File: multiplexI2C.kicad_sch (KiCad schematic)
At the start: 27 parts, among them J17 Conn_01x04_Pin, J18 PinSocket_1x20_P2.54mm_Vertic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, J19 PinSocket_1x20_P2.54mm_Vertic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, J20 Screw_Terminal_01x02, J9 header_0.25sqmm_1x04_P4.2mm_D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, U1 TCA9548A

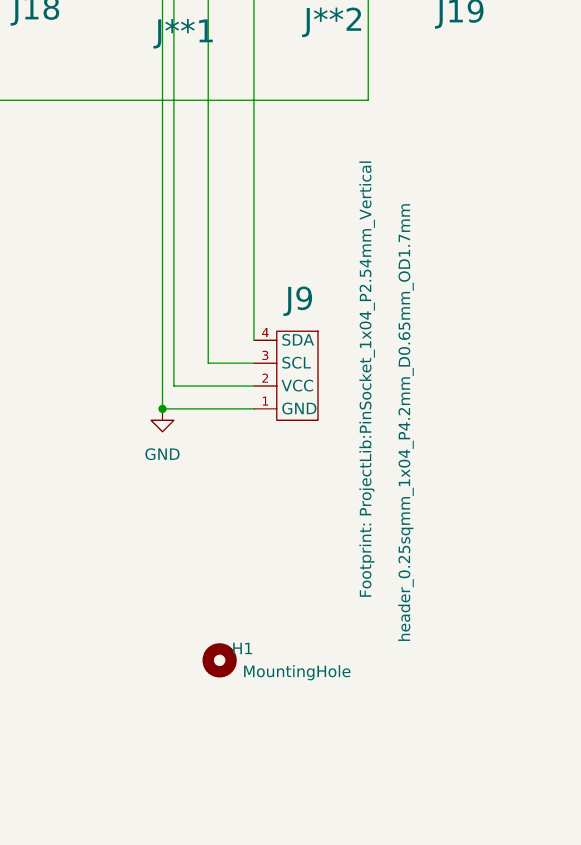
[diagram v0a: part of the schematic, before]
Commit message: cleaning up details forbetter BOM generator.
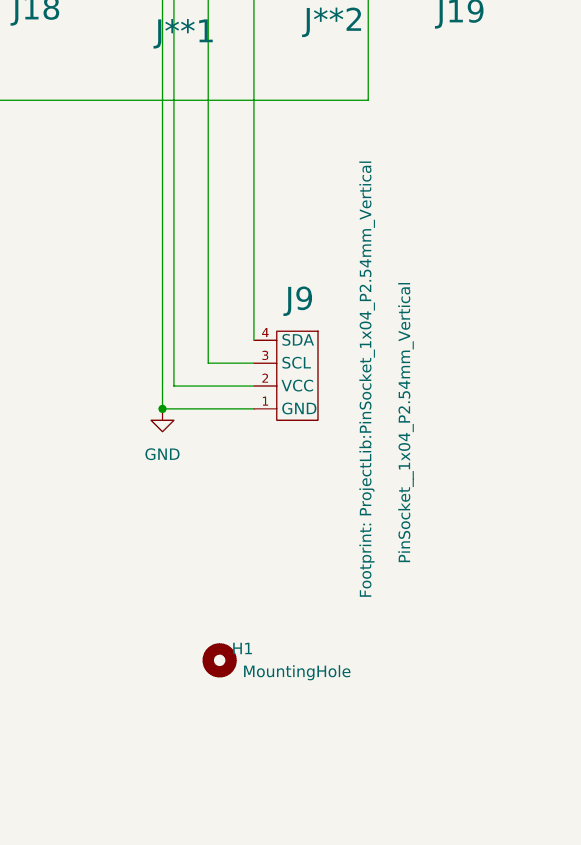
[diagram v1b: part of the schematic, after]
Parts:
- H1, H2, H3, H4, J**1, J**2: now left out of the parts list
- J9: value header_0.25sqmm_1x04_P4.2mm_D0.65mm_OD1.7mm -> PinSocket__1x04_P2.54mm_Vertical; Manufacturer (none) -> JILN; MfgPart (none) -> 228050104ANG1SYA01; MountType (none) -> PTH; Notes (none) -> or equivalent
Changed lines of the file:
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@@
 			)
 		)
-		(property "Description" "one side of blackpill (stm32f401) pins 21-40"
+		(property "Description" "20P header (for blackpill)"
 			(at 207.01 128.27 0)
 			(effects
@@
 			)
 		)
-		(property "Description" "one side of blackpill (stm32f401) pins 1-20"
+		(property "Description" "20P header (for blackpill)"
 			(at 157.48 128.27 0)
 			(effects
@@
 		(unit 1)
 		(exclude_from_sim no)
-		(in_bom yes)
+		(in_bom no)
 		(on_board yes)
 		(dnp no)
@@
 		(unit 1)
 		(exclude_from_sim no)
-		(in_bom yes)
+		(in_bom no)
 		(on_board yes)
 		(dnp no)
@@
 			)
 		)
-		(property "Description" "extra takeoff pads for one side of blackpill (stm32f401) pins 1-20"
+		(property "Description" "unpopulated connections"
 			(at 160.02 128.27 0)
 			(effects
@@
 		(unit 1)
 		(exclude_from_sim no)
-		(in_bom yes)
+		(in_bom no)
 		(on_board yes)
 		(dnp no)
@@
 			)
 		)
-		(property "Value" "header_0.25sqmm_1x04_P4.2mm_D0.65mm_OD1.7mm"
+		(property "Value" "PinSocket__1x04_P2.54mm_Vertical"
 			(at 190.754 200.914 90)
 			(effects
@@
 			)
 		)
-		(property "Description" "4P I2C header for SSD1306 module"
+		(property "Description" "4P header (I2C for SSD1306 module)"
 			(at 165.608 201.676 0)
 			(effects
@@
 			)
 		)
+		(property "Manufacturer" "JILN"
+			(at 176.53 195.58 0)
+			(effects
+				(font
+					(size 1.27 1.27)
+				)
+				(hide yes)
+			)
+		)
+		(property "MfgPart" "228050104ANG1SYA01"
+			(at 176.53 195.58 0)
+			(effects
+				(font
+					(size 1.27 1.27)
+				)
+				(hide yes)
+			)
+		)
+		(property "MountType" "PTH"
+			(at 176.53 195.58 0)
+			(effects
+				(font
+					(size 1.27 1.27)
+				)
+				(hide yes)
+			)
+		)
+		(property "Notes" "or equivalent"
+			(at 176.53 195.58 0)
+			(effects
+				(font
+					(size 1.27 1.27)
+				)
+				(hide yes)
+			)
+		)
 		(pin "4"
 		)
@@
 		(unit 1)
 		(exclude_from_sim no)
-		(in_bom yes)
+		(in_bom no)
 		(on_board yes)
 		(dnp no)
@@
 			)
 		)
-		(property "Description" "extra pads for one side of blackpill (stm32f401) pins 21-40"
+		(property "Description" "unpopulated connections"
 			(at 167.64 128.27 0)
 			(effects
@@
 		(unit 1)
 		(exclude_from_sim no)
-		(in_bom yes)
+		(in_bom no)
 		(on_board yes)
 		(dnp no)
@@
 		(unit 1)
 		(exclude_from_sim no)
-		(in_bom yes)
+		(in_bom no)
 		(on_board yes)
 		(dnp no)
@@
 			)
 		)
-		(property "Description" "Generic connector, single row, 01x04, script generated"
+		(property "Description" "Generic connector, single row, 01x04"
 			(at 199.39 53.34 0)
 			(effects
@@
 			)
 		)
-		(property "Description" "Generic screw terminal, single row, 01x02, script generated (kicad-library-utils/schlib/autogen/connector/)"
+		(property "Description" "Generic screw terminal, single row, 01x02"
 			(at 170.18 73.66 0)
 			(effects

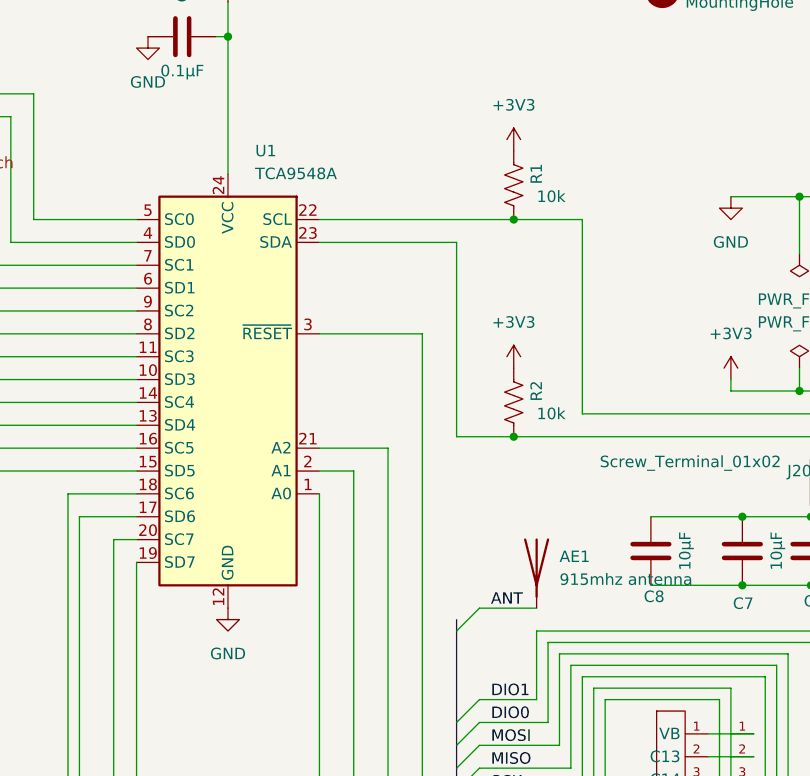
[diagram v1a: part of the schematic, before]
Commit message: as ordered 2024-09 with minor changes for part availability.
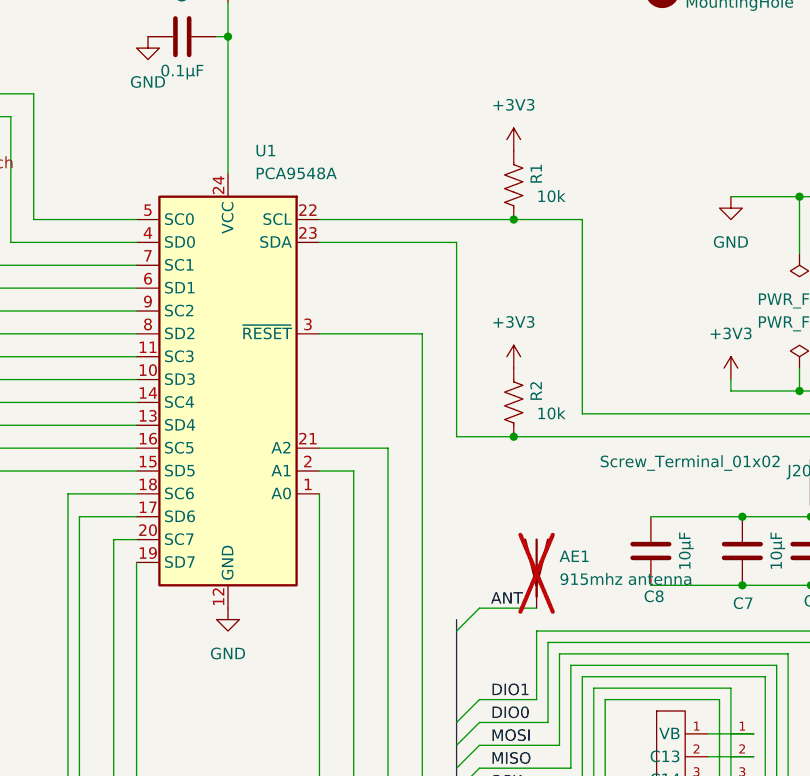
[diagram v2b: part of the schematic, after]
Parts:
- AE1: now not fitted
- U1: value TCA9548A -> PCA9548A; Manufacturer TI -> NXP; MfgPart TCA9548A -> PCA9548APW
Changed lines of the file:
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@@
 			)
 		)
-		(property "Value" "TCA9548A"
+		(property "Value" "PCA9548A"
 			(at 107.1565 40.64 0)
 			(effects
@@
 			)
 		)
-		(property "Datasheet" "http://www.ti.com/lit/ds/symlink/tca9548a.pdf"
+		(property "Datasheet" "https://www.nxp.com/products/interfaces/ic-spi-i3c-interface-devices/ic-logic-multiplexers-switches/eight-channel-ic-bus-switch-with-reset:PCA9548A"
 			(at 102.87 57.15 0)
 			(effects
@@
 			)
 		)
-		(property "Manufacturer" "TI"
+		(property "Manufacturer" "NXP"
 			(at 104.14 63.5 0)
 			(effects
@@
 			)
 		)
-		(property "MfgPart" "TCA9548A"
+		(property "MfgPart" "PCA9548APW"
 			(at 104.14 63.5 0)
 			(effects
@@
 		(in_bom yes)
 		(on_board yes)
-		(dnp no)
+		(dnp yes)
 		(fields_autoplaced yes)
 		(property "Reference" "AE1"

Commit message: minor doc cleanup.
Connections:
- net RESET: now also J**1.7, J18.7 (A1); no longer J**1.6, J18.6 (A0)
- new net: J**1.6, J18.6 (A0)
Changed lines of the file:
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@@
+	)
+	(junction
+		(at 158.75 118.11)
+		(diameter 0)
+		(color 0 0 0 0)
 	)
 	(junction
@@
 	)
 	(junction
-		(at 158.75 115.57)
-		(diameter 0)
-		(color 0 0 0 0)
-	)
-	(junction
 		(at 161.29 78.74)
 		(diameter 0)
@@
 	(wire
 		(pts
-			(xy 158.75 115.57) (xy 162.56 115.57)
-		)
-		(stroke
-			(width 0)
-			(type default)
-		)
-	)
-	(wire
-		(pts
 			(xy 182.88 138.43) (xy 191.77 138.43)
 		)
@@
 	(wire
 		(pts
-			(xy 157.48 118.11) (xy 162.56 118.11)
+			(xy 157.48 118.11) (xy 158.75 118.11)
 		)
 		(stroke
@@
 	(wire
 		(pts
+			(xy 158.75 99.06) (xy 158.75 118.11)
+		)
+		(stroke
+			(width 0)
+			(type default)
+		)
+	)
+	(wire
+		(pts
 			(xy 135.89 45.72) (xy 143.51 45.72)
 		)
@@
 	(wire
 		(pts
-			(xy 158.75 115.57) (xy 158.75 99.06)
-		)
-		(stroke
-			(width 0)
-			(type default)
-		)
-	)
-	(wire
-		(pts
 			(xy 49.53 142.24) (xy 86.36 142.24)
 		)
@@
 	(wire
 		(pts
-			(xy 157.48 115.57) (xy 158.75 115.57)
+			(xy 157.48 115.57) (xy 162.56 115.57)
 		)
 		(stroke
@@
 		)
 		(stroke
+			(width 0)
+			(type default)
+		)
+	)
+	(wire
+		(pts
+			(xy 158.75 118.11) (xy 162.56 118.11)
+		)
+		(stroke

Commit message: ongoing add of MCU, etc.
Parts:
- removed AE1: 915mhz antenna, ProjectLib:915MHz_spring_antenna, symbol Device:Antenna
- removed C5, C6, C7, C8: 10µF, ProjectLib:C_0805_2012Metric, symbol ProjectLib:C
- removed J**1: SolderWire-0.25sqmm_1x20_P4.2mm_D0.65mm_OD1.7mm, ProjectLib:b_pill_takeoffPads_1-20, symbol ProjectLib:b_pill_takeoff_1-20
- removed J**2: SolderWire-0.25sqmm_1x20_P4.2mm_D0.65mm_OD1.7mm, ProjectLib:b_pill_takeoffPads_21-40, symbol ProjectLib:b_pill_takeoff_21-40
- removed J17: Conn_01x04_Pin, ProjectLib:JST_XH_B4B-XH-A_1x04_P2.50mm_Vertical, symbol ProjectLib:Conn_01x04_Pin
- removed J18: PinSocket_1x20_P2.54mm_Vertical, ProjectLib:b_pill_socket_1-20, symbol ProjectLib:b_pill_1-20
- removed J19: PinSocket_1x20_P2.54mm_Vertical, ProjectLib:b_pill_socket_21-40, symbol ProjectLib:b_pill_21-40
- removed J20: Screw_Terminal_01x02, ProjectLib:TerminalBlock_Phoenix_MPT-0,5-2-2.54_1x02_P2.54mm_Horizontal, symbol ProjectLib:Screw_Terminal_01x02
- R1, R2: value 10k -> 10k 1%
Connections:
- net SCL1 is gone; now on net SCL2: R1.2, U1.22 (SCL)
- net SDA1 is gone; now on net SDA2: R2.2, U1.23 (SDA)
- net SCL2: no longer J9.3 (SCL)
- net SDA2: no longer J9.4 (SDA)
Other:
- added sheet f411 (f411.kicad_sch)
- added sheet power (power.kicad_sch)
- moved on the sheet: R3

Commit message: ongoing...
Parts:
- removed J9: PinSocket__1x04_P2.54mm_Vertical, ProjectLib:PinSocket_1x04_P2.54mm_Vertical, symbol ProjectLib:ssd1306_header
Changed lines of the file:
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@@
 	(wire
 		(pts
-			(xy 165.1 196.85) (xy 173.99 196.85)
-		)
-		(stroke
-			(width 0)
-			(type default)
-		)
-	)
-	(wire
-		(pts
 			(xy 118.11 73.66) (xy 118.11 191.77)
 		)
@@
 	(wire
 		(pts
-			(xy 163.83 199.39) (xy 173.99 199.39)
-		)
-		(stroke
-			(width 0)
-			(type default)
-		)
-	)
-	(wire
-		(pts
 			(xy 91.44 163.83) (xy 91.44 81.28)
 		)
@@
 	(wire
 		(pts
-			(xy 168.91 194.31) (xy 173.99 194.31)
-		)
-		(stroke
-			(width 0)
-			(type default)
-		)
-	)
-	(wire
-		(pts
 			(xy 49.53 142.24) (xy 86.36 142.24)
 		)
@@
 	)
 	(symbol
-		(lib_id "ProjectLib:ssd1306_header")
-		(at 176.53 195.58 0)
-		(mirror y)
-		(unit 1)
-		(exclude_from_sim no)
-		(in_bom yes)
-		(on_board yes)
-		(dnp no)
-		(property "Reference" "J9"
-			(at 179.07 187.198 0)
-			(effects
-				(font
-					(size 2.54 2.54)
-				)
-			)
-		)
-		(property "Value" "PinSocket__1x04_P2.54mm_Vertical"
-			(at 190.754 200.914 90)
-			(effects
-				(font
-					(size 1.27 1.27)
-				)
-			)
-		)
-		(property "Footprint" "ProjectLib:PinSocket_1x04_P2.54mm_Vertical"
-			(at 186.436 196.088 90)
-			(show_name yes)
-			(effects
-				(font
-					(size 1.27 1.27)
-				)
-			)
-		)
-		(property "Datasheet" ""
-			(at 151.384 197.866 0)
-			(effects
-				(font
-					(size 1.27 1.27)
-				)
-				(hide yes)
-			)
-		)
-		(property "Description" "4P header (I2C for SSD1306 module)"
-			(at 165.608 201.676 0)
-			(effects
-				(font
-					(size 1.27 1.27)
-				)
-				(hide yes)
-			)
-		)
-		(property "Manufacturer" "JILN"
-			(at 176.53 195.58 0)
-			(effects
-				(font
-					(size 1.27 1.27)
-				)
-				(hide yes)
-			)
-		)
-		(property "MfgPart" "228050104ANG1SYA01"
-			(at 176.53 195.58 0)
-			(effects
-				(font
-					(size 1.27 1.27)
-				)
-				(hide yes)
-			)
-		)
-		(property "MountType" "PTH"
-			(at 176.53 195.58 0)
-			(effects
-				(font
-					(size 1.27 1.27)
-				)
-				(hide yes)
-			)
-		)
-		(property "Notes" "or equivalent"
-			(at 176.53 195.58 0)
-			(effects
-				(font
-					(size 1.27 1.27)
-				)
-				(hide yes)
-			)
-		)
-		(pin "4"
-		)
-		(pin "3"
-		)
-		(pin "2"
-		)
-		(pin "1"
-		)
-		(instances
-			(project ""
-				(path "/0c2d0c14-8850-4a30-bb78-b2f40cb442ba"
-					(reference "J9")
-					(unit 1)
-				)
-			)
-		)
-	)
-	(symbol
 		(lib_id "power:GND")
 		(at 95.25 25.4 0)
@@
 	)
 	(symbol
-		(lib_id "power:GND")
-		(at 163.83 199.39 0)
-		(unit 1)
-		(exclude_from_sim no)
-		(in_bom yes)
-		(on_board yes)
-		(dnp no)
-		(fields_autoplaced yes)
-		(property "Reference" "#PWR049"
-			(at 163.83 205.74 0)
-			(effects
-				(font
-					(size 1.27 1.27)
-				)
-				(hide yes)
-			)
-		)
-		(property "Value" "GND"
-			(at 163.83 204.47 0)
-			(effects
-				(font
-					(size 1.27 1.27)
-				)
-			)
-		)
-		(property "Footprint" ""
-			(at 163.83 199.39 0)
-			(effects
-				(font
-					(size 1.27 1.27)
-				)
-				(hide yes)
-			)
-		)
-		(property "Datasheet" ""
-			(at 163.83 199.39 0)
-			(effects
-				(font
-					(size 1.27 1.27)
-				)
-				(hide yes)
-			)
-		)
-		(property "Description" "Power symbol creates a global label with name \"GND\" , ground"
-			(at 163.83 199.39 0)
-			(effects
-				(font
-					(size 1.27 1.27)
-				)
-				(hide yes)
-			)
-		)
-		(pin "1"
-		)
-		(instances
-			(project "multiplexI2CwithRJ11"
-				(path "/0c2d0c14-8850-4a30-bb78-b2f40cb442ba"
-					(reference "#PWR049")
-					(unit 1)
-				)
-			)
-		)
-	)
-	(symbol
 		(lib_id "ProjectLib:TCA9548APWR")
 		(at 104.14 63.5 0)
@@
 	)
 	(sheet
-		(at 139.7 109.22)
+		(at 156.21 110.49)
 		(size 31.75 39.37)
 		(exclude_from_sim no)
@@
 		)
 		(property "Sheetname" "f411"
-			(at 139.7 108.5084 0)
+			(at 156.21 109.7784 0)
 			(effects
 				(font
@@
 		)
 		(property "Sheetfile" "f411.kicad_sch"
-			(at 139.7 149.1746 0)
+			(at 156.21 150.4446 0)
 			(effects
 				(font
@@
 	)
 	(sheet
-		(at 35.56 191.77)
+		(at 161.29 168.91)
 		(size 25.4 41.91)
 		(exclude_from_sim no)
@@
 		)
 		(property "Sheetname" "RFM95W"
-			(at 35.56 191.0584 0)
+			(at 161.29 168.1984 0)
 			(effects
 				(font
@@
 		)
 		(property "Sheetfile" "RFM95W.kicad_sch"
-			(at 37.084 186.944 0)
+			(at 162.814 164.084 0)
 			(effects
 				(font
